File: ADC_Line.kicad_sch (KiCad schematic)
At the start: 3 parts

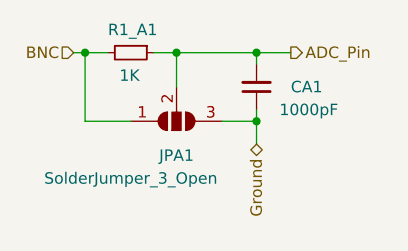
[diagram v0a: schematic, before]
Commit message: KiCad 7.0 SPI_CS3 Reste simplification du chemin Redondance alim +5V
Mais surtout KiCad 7.0 qui empêche la rétrocompatibilité avec les version antérieure sous KiCad 6.x

git-svn-id: file:///D%5C00%20-%20Dev%20&%20Calculs%5CRepoTortoiseSVN_PCB%5CCANduino128/branches/CANduino128%20-%20v4.0a@84 67ddf66f-3787-a644-8df7-7746e21a92b3
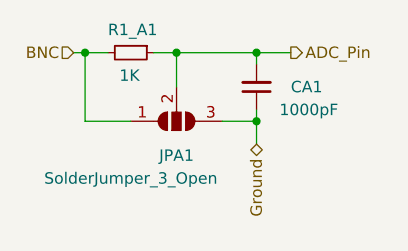
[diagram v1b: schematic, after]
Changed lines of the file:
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@@
-(kicad_sch (version 20211123) (generator eeschema)
+(kicad_sch (version 20230121) (generator eeschema)
   (paper "A4")
   (junction (at 125.73 72.39) (diameter 0) (color 0 0 0 0)
@@
   )
   (wire (pts (xy 134.62 73.66) (xy 134.62 72.39))
-    (stroke (width 0) (type default) (color 0 0 0 0))
+    (stroke (width 0) (type default))
   )
   (wire (pts (xy 134.62 78.74) (xy 134.62 80.01))
-    (stroke (width 0) (type default) (color 0 0 0 0))
+    (stroke (width 0) (type default))
   )
   (wire (pts (xy 125.73 76.2) (xy 125.73 72.39))
-    (stroke (width 0) (type default) (color 0 0 0 0))
+    (stroke (width 0) (type default))
   )
   (wire (pts (xy 134.62 72.39) (xy 138.43 72.39))
-    (stroke (width 0) (type default) (color 0 0 0 0))
+    (stroke (width 0) (type default))
   )
   (wire (pts (xy 130.81 80.01) (xy 134.62 80.01))
-    (stroke (width 0) (type default) (color 0 0 0 0))
+    (stroke (width 0) (type default))
   )
   (wire (pts (xy 115.57 72.39) (xy 118.11 72.39))
-    (stroke (width 0) (type default) (color 0 0 0 0))
+    (stroke (width 0) (type default))
   )
   (wire (pts (xy 125.73 72.39) (xy 134.62 72.39))
-    (stroke (width 0) (type default) (color 0 0 0 0))
+    (stroke (width 0) (type default))
   )
   (wire (pts (xy 115.57 80.01) (xy 120.65 80.01))
-    (stroke (width 0) (type default) (color 0 0 0 0))
+    (stroke (width 0) (type default))
   )
   (wire (pts (xy 134.62 80.01) (xy 134.62 82.55))
-    (stroke (width 0) (type default) (color 0 0 0 0))
+    (stroke (width 0) (type default))
   )
   (wire (pts (xy 115.57 80.01) (xy 115.57 72.39))
-    (stroke (width 0) (type default) (color 0 0 0 0))
+    (stroke (width 0) (type default))
   )
   (wire (pts (xy 114.3 72.39) (xy 115.57 72.39))
-    (stroke (width 0) (type default) (color 0 0 0 0))
+    (stroke (width 0) (type default))
   )
   (wire (pts (xy 123.19 72.39) (xy 125.73 72.39))
-    (stroke (width 0) (type default) (color 0 0 0 0))
+    (stroke (width 0) (type default))
   )
-  (hierarchical_label "ADC_Pin" (shape output) (at 138.43 72.39 0)
+  (hierarchical_label "ADC_Pin" (shape output) (at 138.43 72.39 0) (fields_autoplaced)
     (effects (font (size 1.27 1.27)) (justify left))
   )
-  (hierarchical_label "BNC" (shape input) (at 114.3 72.39 180)
+  (hierarchical_label "BNC" (shape input) (at 114.3 72.39 180) (fields_autoplaced)
     (effects (font (size 1.27 1.27)) (justify right))
   )
-  (hierarchical_label "Ground" (shape bidirectional) (at 134.62 82.55 270)
+  (hierarchical_label "Ground" (shape bidirectional) (at 134.62 82.55 270) (fields_autoplaced)
     (effects (font (size 1.27 1.27)) (justify right))
   )
   (symbol (lib_id "Jumper:SolderJumper_3_Open") (at 125.73 80.01 0) (mirror x) (unit 1)
-    (in_bom yes) (on_board yes)
-    (property "Reference" "JPA1" (id 0) (at 125.73 83.82 0))
-    (property "Value" "SolderJumper_3_Open" (id 1) (at 120.65 86.36 0))
-    (property "Footprint" "Jumper:SolderJumper-3_P1.3mm_Open_RoundedPad1.0x1.5mm" (id 2) (at 125.73 80.01 0)
+    (in_bom yes) (on_board yes) (dnp no)
+    (property "Reference" "JPA1" (at 125.73 83.82 0)
+      (effects (font (size 1.27 1.27)))
+    )
+    (property "Value" "SolderJumper_3_Open" (at 120.65 86.36 0)
+      (effects (font (size 1.27 1.27)))
+    )
+    (property "Footprint" "Jumper:SolderJumper-3_P1.3mm_Open_RoundedPad1.0x1.5mm" (at 125.73 80.01 0)
       (effects (font (size 1.27 1.27)) hide)
     )
-    (property "Datasheet" "~" (id 3) (at 125.73 80.01 0)
+    (property "Datasheet" "~" (at 125.73 80.01 0)
       (effects (font (size 1.27 1.27)) hide)
     )
@@
     (pin "2")
     (pin "3")
+    (instances
+      (project "CANduino128"
+        (path "/b26d10c1-0874-459a-80a4-e525262e670c/e9cdc009-408c-49cc-a9aa-b5ab6d61a947"
+          (reference "JPA1") (unit 1)
+        )
+        (path "/b26d10c1-0874-459a-80a4-e525262e670c/f8348586-92ee-4a19-86a2-b6a6c4962eeb"
+          (reference "JPA2") (unit 1)
+        )
+        (path "/b26d10c1-0874-459a-80a4-e525262e670c/e1e65187-f0ac-4790-b174-b0b45635262c"
+          (reference "JPA3") (unit 1)
+        )
+        (path "/b26d10c1-0874-459a-80a4-e525262e670c/70f44b0f-5019-41d8-8648-92b0c45a7470"
+          (reference "JPA4") (unit 1)
+        )
+        (path "/b26d10c1-0874-459a-80a4-e525262e670c/938591d5-c204-42f9-a976-01b8222bb8ab"
+          (reference "JPA5") (unit 1)
+        )
+        (path "/b26d10c1-0874-459a-80a4-e525262e670c/658debcc-1850-4b00-b26b-8bfc70eb5dfd"
+          (reference "JPA6") (unit 1)
+        )
+        (path "/b26d10c1-0874-459a-80a4-e525262e670c/0e723a67-ff7d-4409-b0c6-f3101e04248b"
+          (reference "JPA7") (unit 1)
+        )
+        (path "/b26d10c1-0874-459a-80a4-e525262e670c/d2dfb9cd-7f26-40ed-b95a-1822496f5075"
+          (reference "JPA8") (unit 1)
+        )
+      )
+    )
   )
   (symbol (lib_id "Device:R_Small") (at 120.65 72.39 270) (unit 1)
-    (in_bom yes) (on_board yes)
-    (property "Reference" "R1_A1" (id 0) (at 118.11 69.85 90)
+    (in_bom yes) (on_board yes) (dnp no)
+    (property "Reference" "R1_A1" (at 118.11 69.85 90)
       (effects (font (size 1.27 1.27)) (justify left))
     )
-    (property "Value" "1K" (id 1) (at 119.38 74.93 90)
+    (property "Value" "1K" (at 119.38 74.93 90)
       (effects (font (size 1.27 1.27)) (justify left))
     )
-    (property "Footprint" "Resistor_SMD:R_1210_3225Metric_Pad1.30x2.65mm_HandSolder" (id 2) (at 120.65 72.39 0)
+    (property "Footprint" "Resistor_SMD:R_1210_3225Metric_Pad1.30x2.65mm_HandSolder" (at 120.65 72.39 0)
       (effects (font (size 1.27 1.27)) hide)
     )
-    (property "Datasheet" "~" (id 3) (at 120.65 72.39 0)
+    (property "Datasheet" "~" (at 120.65 72.39 0)
       (effects (font (size 1.27 1.27)) hide)
     )
     (pin "1")
     (pin "2")
+    (instances
+      (project "CANduino128"
+        (path "/b26d10c1-0874-459a-80a4-e525262e670c/e9cdc009-408c-49cc-a9aa-b5ab6d61a947"
+          (reference "R1_A1") (unit 1)
+        )
+        (path "/b26d10c1-0874-459a-80a4-e525262e670c/f8348586-92ee-4a19-86a2-b6a6c4962eeb"
+          (reference "R1_A2") (unit 1)
+        )
+        (path "/b26d10c1-0874-459a-80a4-e525262e670c/e1e65187-f0ac-4790-b174-b0b45635262c"
+          (reference "R1_A3") (unit 1)
+        )
+        (path "/b26d10c1-0874-459a-80a4-e525262e670c/70f44b0f-5019-41d8-8648-92b0c45a7470"
+          (reference "R1_A4") (unit 1)
+        )
+        (path "/b26d10c1-0874-459a-80a4-e525262e670c/938591d5-c204-42f9-a976-01b8222bb8ab"
+          (reference "R1_A5") (unit 1)
+        )
+        (path "/b26d10c1-0874-459a-80a4-e525262e670c/658debcc-1850-4b00-b26b-8bfc70eb5dfd"
+          (reference "R1_A6") (unit 1)
+        )
+        (path "/b26d10c1-0874-459a-80a4-e525262e670c/0e723a67-ff7d-4409-b0c6-f3101e04248b"
+          (reference "R1_A7") (unit 1)
+        )
+        (path "/b26d10c1-0874-459a-80a4-e525262e670c/d2dfb9cd-7f26-40ed-b95a-1822496f5075"
+          (reference "R1_A8") (unit 1)
+        )
+      )
+    )
   )
   (symbol (lib_id "Device:C_Small") (at 134.62 76.2 180) (unit 1)
-    (in_bom yes) (on_board yes)
-    (property "Reference" "CA1" (id 0) (at 138.43 76.2 0)
+    (in_bom yes) (on_board yes) (dnp no)
+    (property "Reference" "CA1" (at 138.43 76.2 0)
       (effects (font (size 1.27 1.27)) (justify right))
     )
-    (property "Value" "1000pF" (id 1) (at 137.16 78.74 0)
+    (property "Value" "1000pF" (at 137.16 78.74 0)
       (effects (font (size 1.27 1.27)) (justify right))
     )
-    (property "Footprint" "Capacitor_SMD:C_1210_3225Metric_Pad1.33x2.70mm_HandSolder" (id 2) (at 134.62 76.2 0)
+    (property "Footprint" "Capacitor_SMD:C_1210_3225Metric_Pad1.33x2.70mm_HandSolder" (at 134.62 76.2 0)
       (effects (font (size 1.27 1.27)) hide)
     )
-    (property "Datasheet" "~" (id 3) (at 134.62 76.2 0)
+    (property "Datasheet" "~" (at 134.62 76.2 0)
       (effects (font (size 1.27 1.27)) hide)
     )
     (pin "1")
     (pin "2")
+    (instances
+      (project "CANduino128"
+        (path "/b26d10c1-0874-459a-80a4-e525262e670c/e9cdc009-408c-49cc-a9aa-b5ab6d61a947"
+          (reference "CA1") (unit 1)
+        )
+        (path "/b26d10c1-0874-459a-80a4-e525262e670c/f8348586-92ee-4a19-86a2-b6a6c4962eeb"
+          (reference "CA2") (unit 1)
+        )
+        (path "/b26d10c1-0874-459a-80a4-e525262e670c/e1e65187-f0ac-4790-b174-b0b45635262c"
+          (reference "CA3") (unit 1)
+        )
+        (path "/b26d10c1-0874-459a-80a4-e525262e670c/70f44b0f-5019-41d8-8648-92b0c45a7470"
+          (reference "CA4") (unit 1)
+        )
+        (path "/b26d10c1-0874-459a-80a4-e525262e670c/938591d5-c204-42f9-a976-01b8222bb8ab"
+          (reference "CA5") (unit 1)
+        )
+        (path "/b26d10c1-0874-459a-80a4-e525262e670c/658debcc-1850-4b00-b26b-8bfc70eb5dfd"
+          (reference "CA6") (unit 1)
+        )
+        (path "/b26d10c1-0874-459a-80a4-e525262e670c/0e723a67-ff7d-4409-b0c6-f3101e04248b"
+          (reference "CA7") (unit 1)
+        )
+        (path "/b26d10c1-0874-459a-80a4-e525262e670c/d2dfb9cd-7f26-40ed-b95a-1822496f5075"
+          (reference "CA8") (unit 1)
+        )
+      )
+    )
   )
 )
